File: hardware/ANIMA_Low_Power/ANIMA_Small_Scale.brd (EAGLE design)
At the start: 50 x 48.3 mm, 65 parts, among them J1 POW_CONNECTFEMALE-RA, Q1 MOSFET-PCHANNELSMD, Q2 MOSFET-PCHANNELSMD, Q3 MOSFET-PCHANNELSMD, Q4 MOSFET-PCHANNELSMD, Q5 MOSFET-PCHANNELSMD, Q6 MOSFET-PCHANNELSMD, U1 PIC32MX20F***B-44PIN, U12 MICRO-SDCARDSOCKET, U2 TPS54040, U3 MEDIATEK-3329, U4 TC1047, U5 MMA8451Q, U6 MAG3110

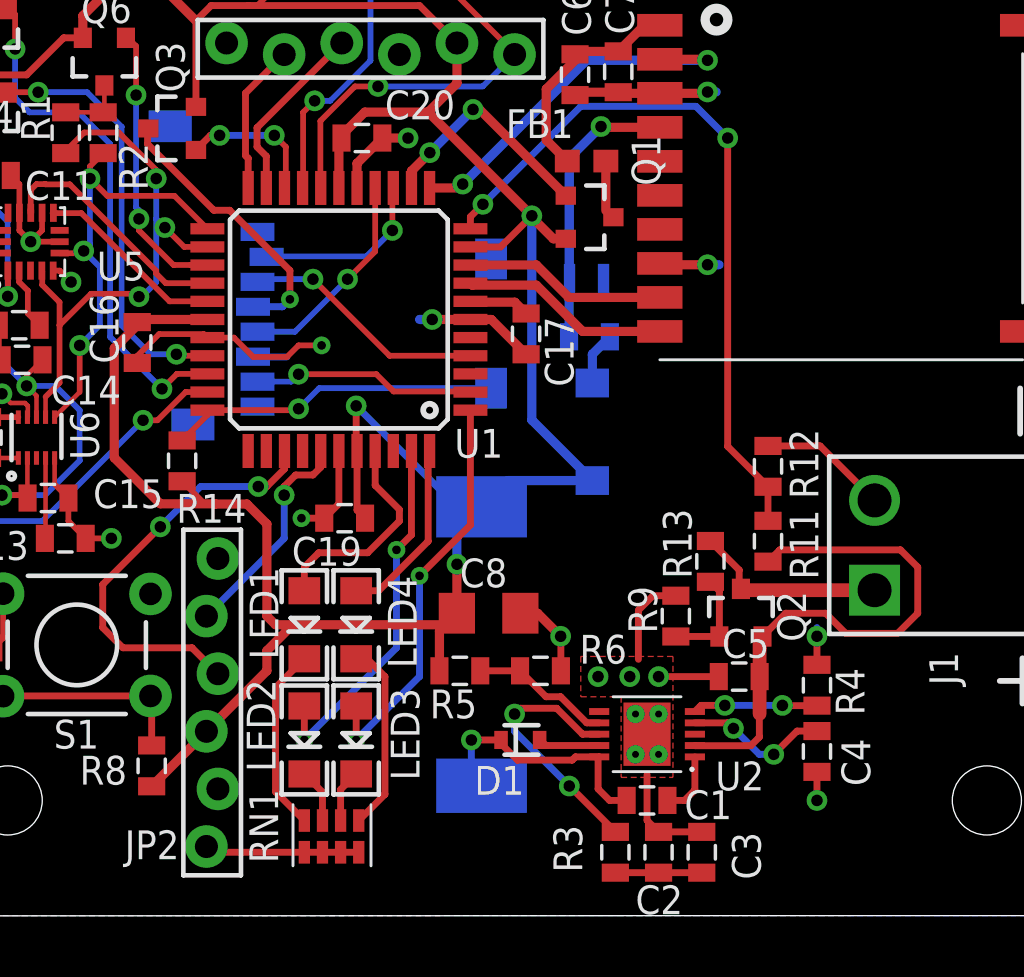
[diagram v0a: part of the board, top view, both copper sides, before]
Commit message: creation of package for new processor replaced high power with low and reconnected major connections
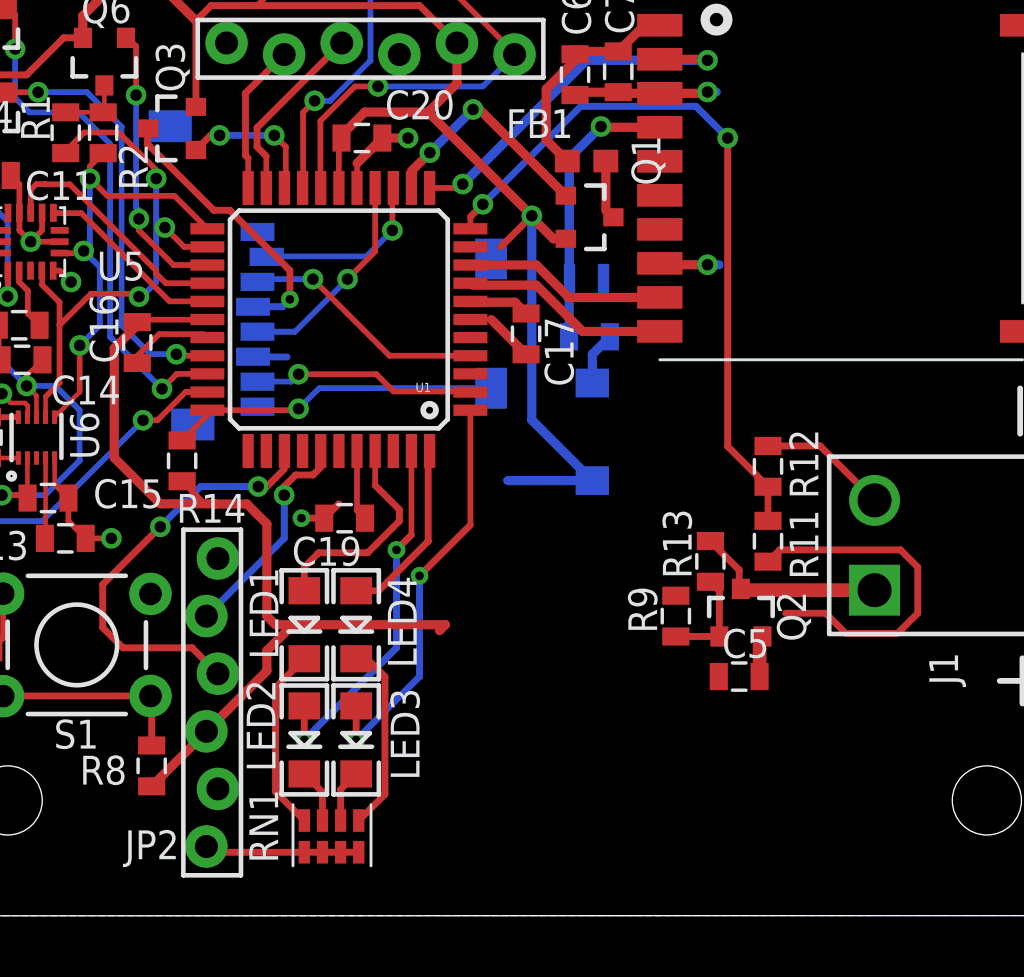
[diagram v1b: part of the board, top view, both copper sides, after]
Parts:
- removed C1: .1u, ANIMAlib:0805
- removed C2: 47p, ANIMAlib:0805
- removed C3: .018u, ANIMAlib:0805
- removed C4: .015u, ANIMAlib:0805
- removed C8: 10u, ANIMAlib:1206
- removed D1: (no value), ANIMAlib:SOD523
- removed L1: 68uH, ANIMAlib:ELL-CTVV
- removed R3: 15.8K, ANIMAlib:0805
- removed R4: 165K, ANIMAlib:0805
- removed R5: 31.6K, ANIMAlib:0805
- removed R6: 10K, ANIMAlib:0805
- removed U2: TPS54040, ANIMAlib:MSOP-10-GNDPAD
- U1: value PIC32MX20F***B-44PIN -> PIC24FJXXXGA204-44PIN
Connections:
- removed net N$10: R5.1, R6.2, U2.7
- removed net N$14: R4.2, U2.5
- removed net N$15: C4.2, U2.4
- removed net N$5: C1.1, D1.+, L1.P$1, U2.10
- removed net N$6: C2.1, C3.2, R3.1
- removed net N$8: R3.2, U2.8
- new net N$24: C5.2, Q2.2
- net GND: no longer C2.2, C3.1, C4.1, C8.2, D1.-, R4.1, R6.1, U1.6, U2.9, U2.GND, U2.GND@1, U2.GND@2, U2.GND@3, U2.GND@4
- net N$4: now also U1.34; no longer C1.2, U2.1
- net VBAT: no longer C5.2, Q2.2, U2.2
- net VCC3V3: no longer C8.1, L1.P$2, R5.2, U1.10
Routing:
- net GND: track 95.9 -> 63.3 mm, vias 18 -> 10
- net VCC3V3: track 141.0 -> 120.8 mm, vias 3 -> 1
- net N$5: track 11.5 -> 0.00 mm, vias 1 -> 0
- net N$8: track 11.4 -> 0.00 mm, vias 2 -> 0
- net VBAT: track 24.7 -> 15.7 mm
- net N$15: track 6.38 -> 0.00 mm, vias 2 -> 0
- net N$10: track 6.20 -> 0.00 mm
- net N$14: track 5.50 -> 0.00 mm, vias 2 -> 0
- net N$6: track 3.81 -> 0.00 mm
- net N$4: track 2.86 -> 0.00 mm
- net N$24: track 0.00 -> 1.82 mm
- removed copper zone on layer 1, net GND

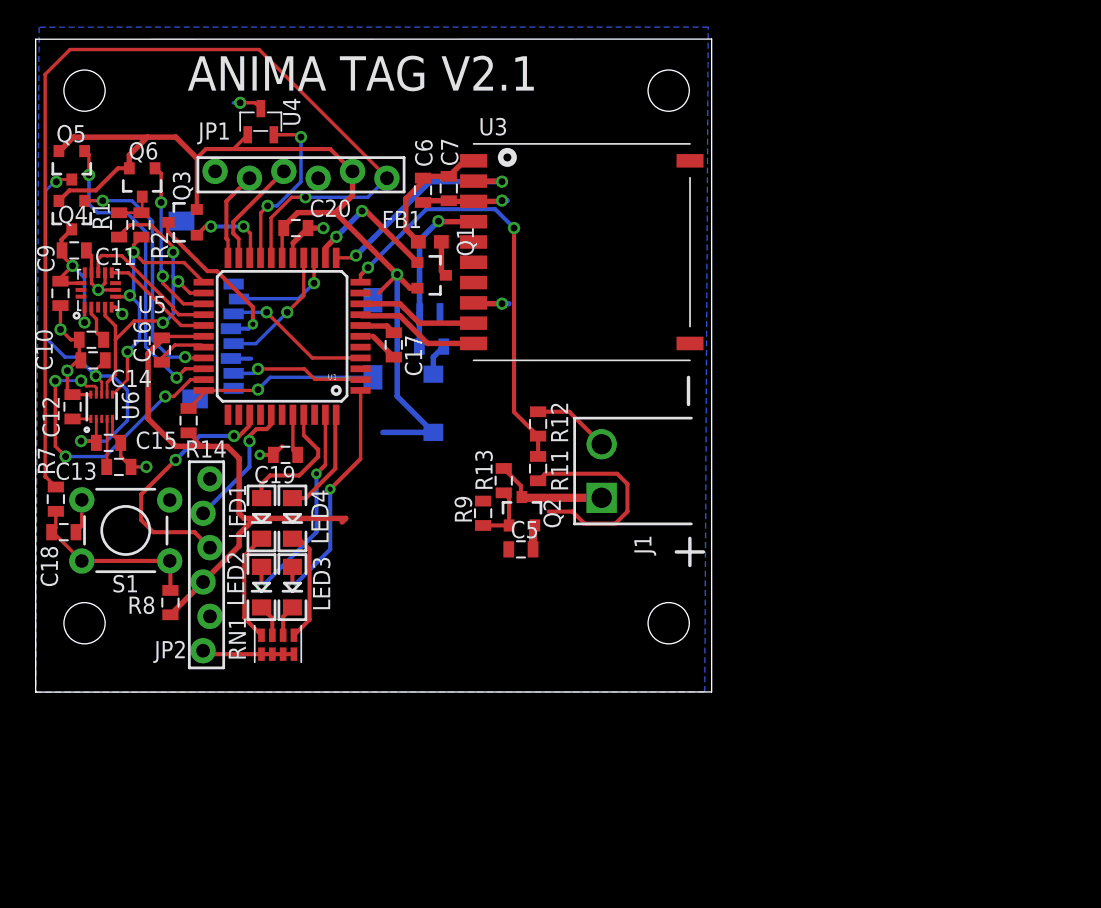
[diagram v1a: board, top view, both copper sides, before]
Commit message: added oscillator removed connections prior to moving GPS to new position added additional parts
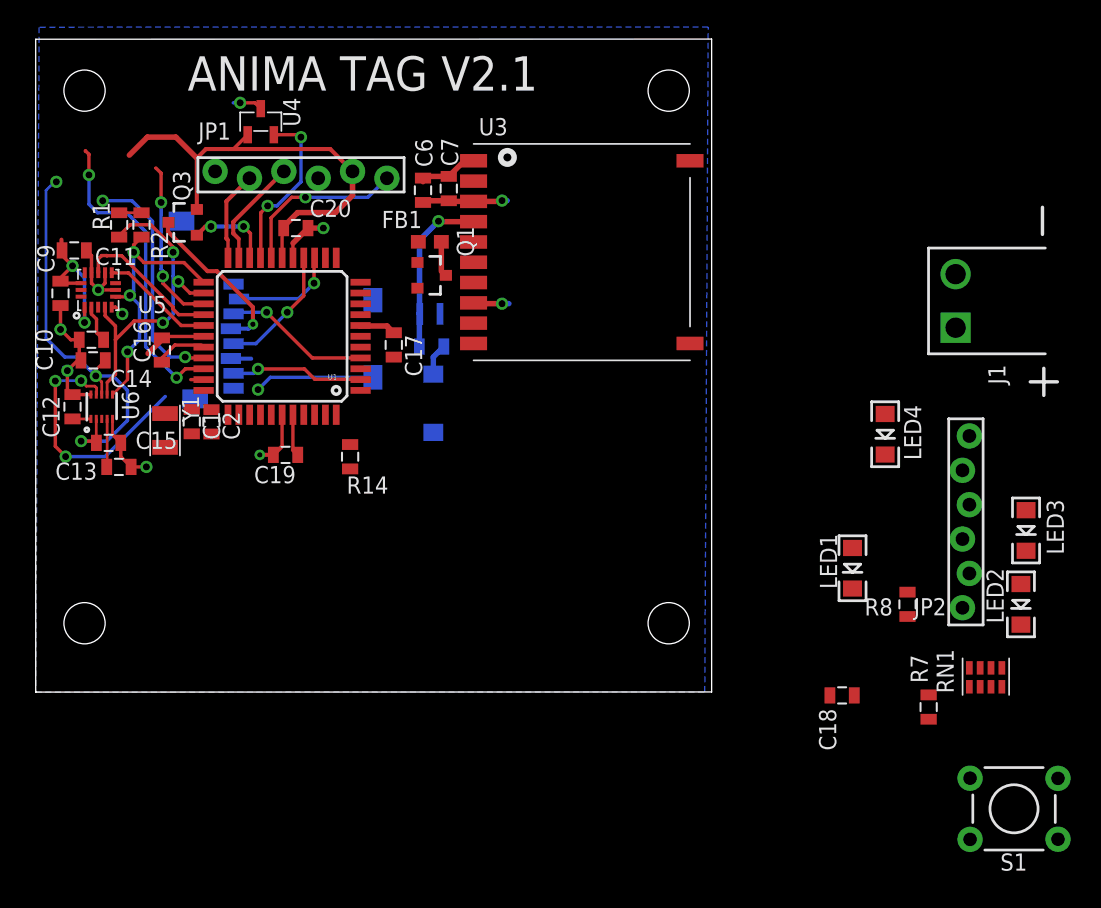
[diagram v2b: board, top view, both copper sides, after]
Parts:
- removed C5: 4.7u, ANIMAlib:0805
- removed Q2, Q4, Q5, Q6: MOSFET-PCHANNELSMD, ANIMAlib:SOT23-3
- removed R11: 30K, ANIMAlib:0805
- removed R12: 7.5K, ANIMAlib:0805
- removed R13: 2M, ANIMAlib:0805
- removed R9: 1.2M, ANIMAlib:0805
- added C1, C2: (no value), ANIMAlib:0805
- added Y1: (no value), ANIMAlib:CRYSTAL-ABS07
- moved S1 68.8 mm to (72.3, -8.63)
- moved R7 66.3 mm to (66.0, -1.11)
- moved C18 58.8 mm to (59.6, -0.24)
- moved JP2 56.2 mm to (68.8, 18.9)
- moved LED2 56.1 mm to (72.8, 6.49)
- moved R8 54.5 mm to (64.4, 6.49)
- moved LED3 54.4 mm to (73.2, 11.9)
- moved RN1 52.4 mm to (69.0, 0.39)
- moved LED4 44.3 mm to (62.8, 19.1)
- moved LED1 43.8 mm to (60.4, 9.15)
- moved J1 29.0 mm to (68.0, 26.9)
- moved R14 12.2 mm to (23.2, 17.4)
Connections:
- removed net ACCEL_POWER_EN: Q4.1, U1.30
- removed net I2C_POWER_EN: Q6.1, U1.25
- removed net MAG_POWER_EN: Q5.1, U1.31
- removed net N$12: Q2.1, R13.1, R9.1
- removed net N$20: J1.1, Q2.3, R13.2
- removed net N$24: C5.2, Q2.2
- removed net N$4: U1.34
- removed net VBAT: R11.2
- new net SOSCI: C1.1, U1.33, Y1.P$1
- new net SOSCO: C2.1, U1.34, Y1.P$2
- net ACCEL_POWER: now also U1.30; no longer Q4.3
- net CD1: no longer U1.33
- net GND: now also C1.2, C2.2; no longer C5.1, R12.1, R9.2
- net I2C_POWER: now also U1.25; no longer Q6.3
- net MAG_POWER: now also U1.31; no longer Q5.3
- net VBAT_SCALED: no longer R11.1, R12.2
- net VCC3V3: now also J1.1; no longer Q4.2, Q5.2, Q6.2
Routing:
- net VCC3V3: track 120.8 -> 42.9 mm, vias 1 -> 0
- net MCLR: track 73.7 -> 12.7 mm
- net VBAT_SCALED: track 32.1 -> 0.00 mm, vias 2 -> 0
- net MAG_POWER_EN: track 23.2 -> 0.00 mm, vias 2 -> 0
- net MAG_POWER: track 33.1 -> 55.2 mm, vias 3 -> 5
- net ACCEL_POWER_EN: track 18.8 -> 0.00 mm, vias 2 -> 0
- net DEBUG_TX: track 18.7 -> 0.00 mm, vias 2 -> 0
- net DLED3: track 18.1 -> 0.00 mm, vias 2 -> 0
- net GPS_EN: track 16.7 -> 0.00 mm, vias 2 -> 0
- net ACCEL_POWER: track 12.6 -> 28.9 mm, vias 2 -> 4
- net DLED2: track 16.2 -> 0.00 mm, vias 2 -> 0
- net VBAT: track 15.7 -> 0.00 mm
- net GND: track 63.3 -> 48.5 mm
- net N$9: track 14.1 -> 0.00 mm
- net I2C_POWER_EN: track 12.4 -> 0.00 mm, vias 2 -> 0
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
